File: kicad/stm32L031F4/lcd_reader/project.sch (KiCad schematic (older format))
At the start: 17 parts, among them J1 WAKE, J13 GND_EXT, J2 SWD, J8 RADIO, Q1 CSD16414Q5, U1 74LS14, U2 STM32L031F4Px, U3 74LS14

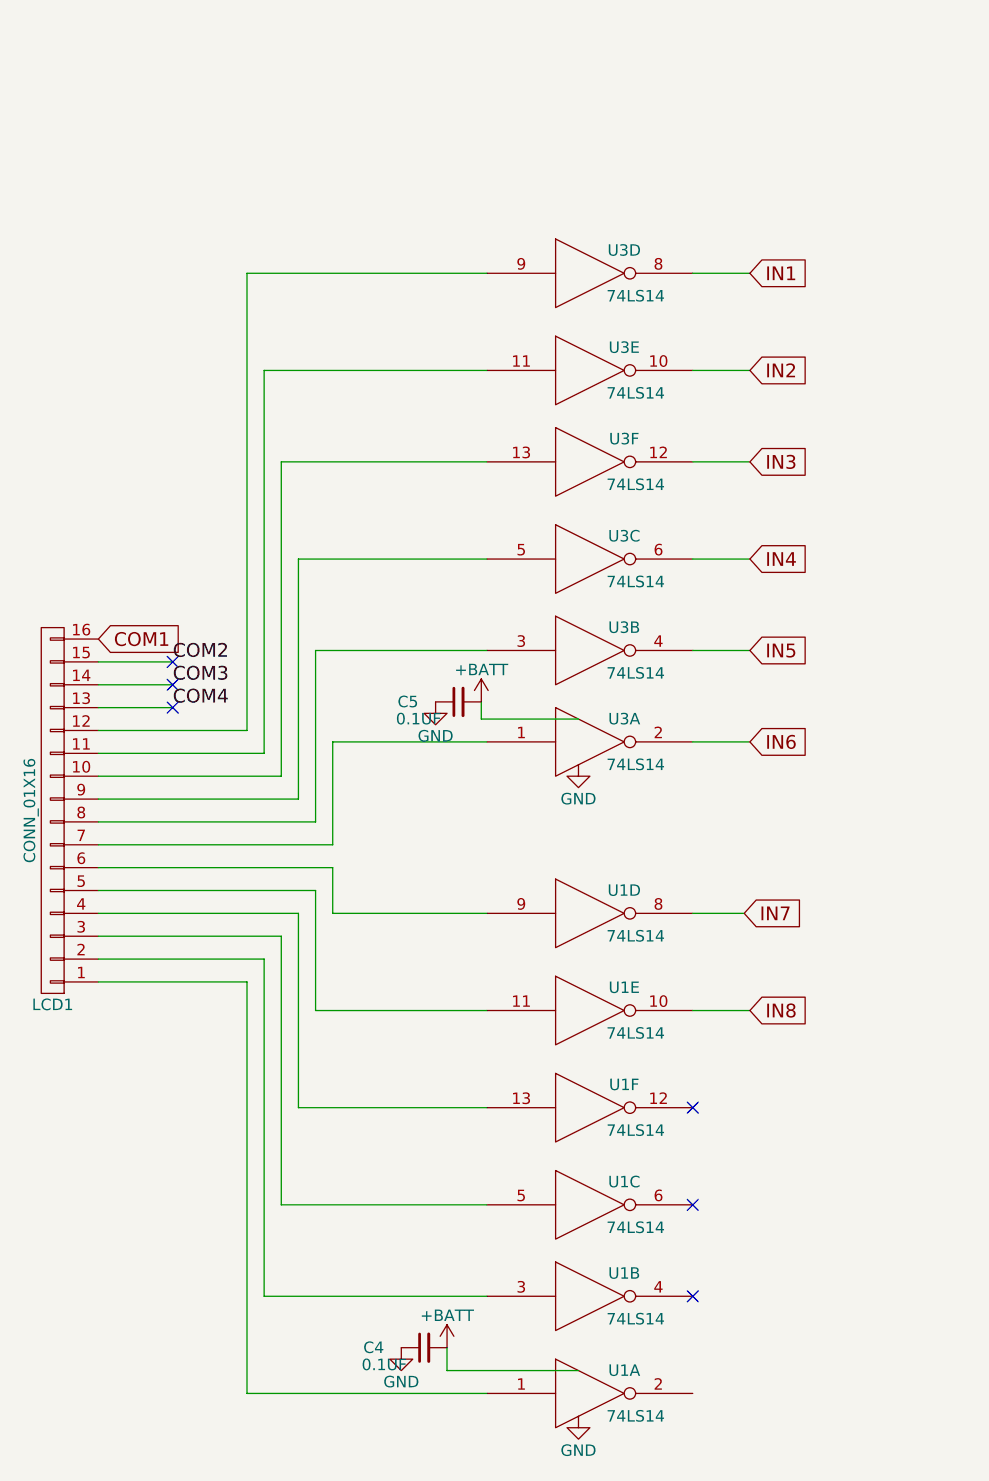
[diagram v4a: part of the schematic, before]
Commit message: SOIC-14 for the schmitt triggers
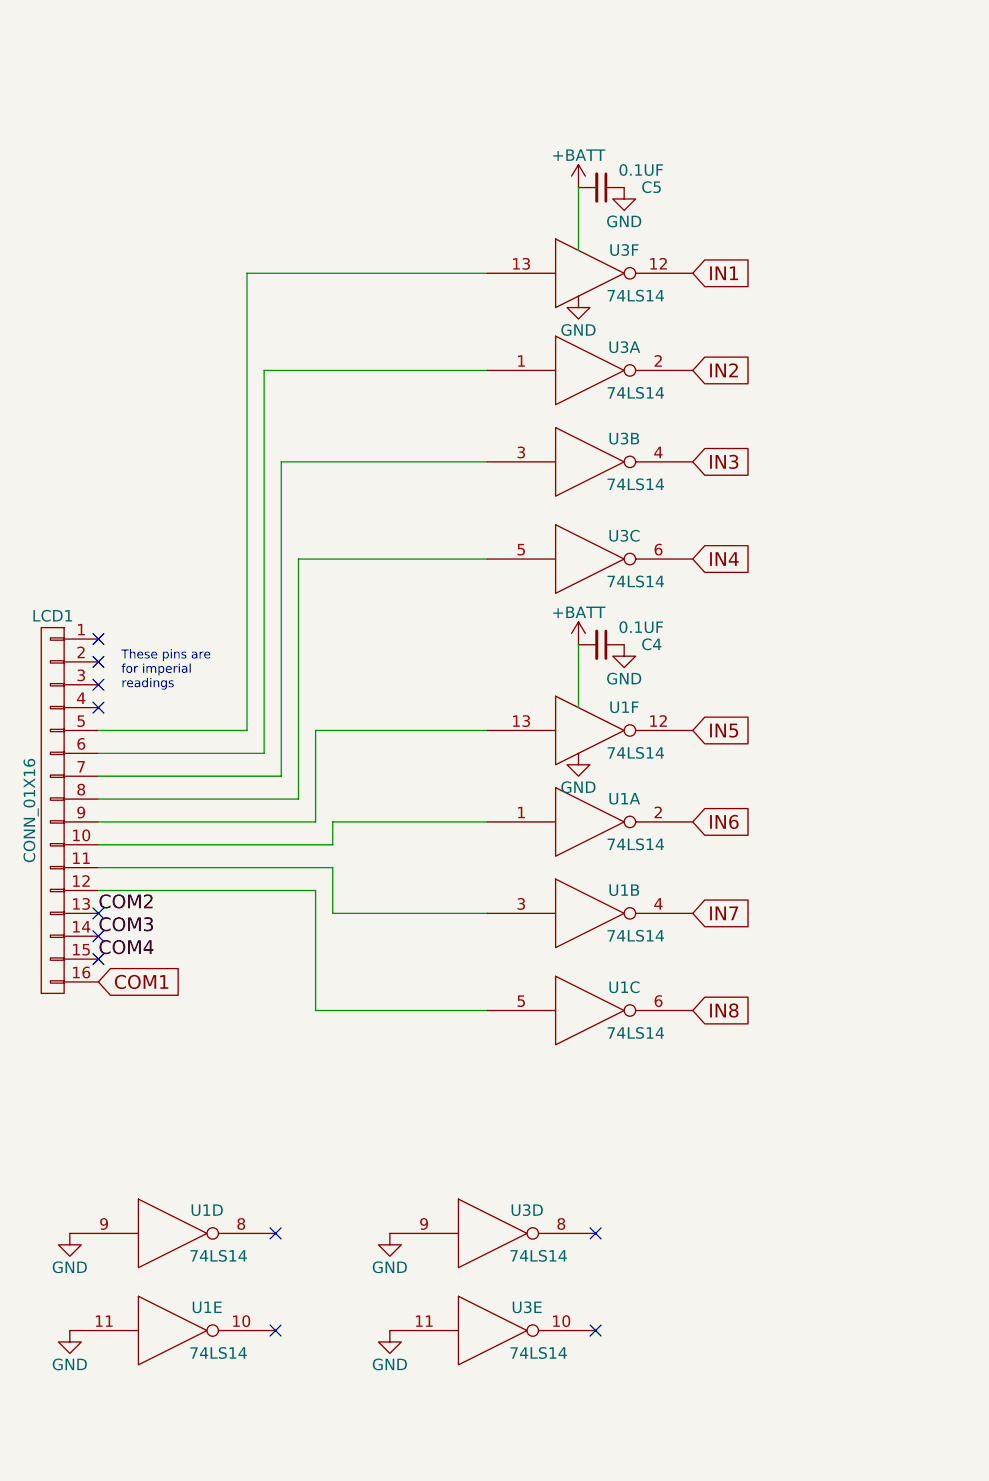
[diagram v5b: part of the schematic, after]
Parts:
- U1, U3: footprint SMD_Packages:SSOP-14 -> Housings_SOIC:SOIC-14_3.9x8.7mm_Pitch1.27mm
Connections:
- net COM2: now also LCD1.13 (P13); no longer LCD1.15 (P15)
- net COM4: now also LCD1.15 (P15); no longer LCD1.13 (P13)
- net GND: now also U1.11, U1.9, U3.11, U3.9
- net IN1: now also U3.12; no longer U3.8
- net IN2: now also U3.2; no longer U3.10
- net IN3: now also U3.4; no longer U3.12
- net IN5: now also U1.12; no longer U3.4
- net IN6: now also U1.2; no longer U3.2
- net IN7: now also U1.4; no longer U1.8
- net IN8: now also U1.6; no longer U1.10
- net at U3.13: now also LCD1.5 (P5); no longer LCD1.10 (P10)
- net at LCD1.11 (P11): now also U1.3; no longer U3.11
- net at LCD1.12 (P12): now also U1.5; no longer U3.9
- net at U3.5: now also LCD1.8 (P8); no longer LCD1.9 (P9)
- net at U1.13: now also LCD1.9 (P9); no longer LCD1.4 (P4)
- net at LCD1.6 (P6): now also U3.1; no longer U1.9
- net at LCD1.3 (P3): no longer U1.5
- net at U3.3: now also LCD1.7 (P7); no longer LCD1.8 (P8)
- net at LCD1.2 (P2): no longer U1.3
- net at U1.1: now also LCD1.10 (P10); no longer LCD1.1 (P1)
- no-connect marks 6 -> 11
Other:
- note added: "These pins are \nfor imperial\nreadings"
- moved on the sheet: C4, C5, U1A, U1B, U1C, U1D, U1E, U1F, U3A, U3B, U3D, U3E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

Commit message: Pull down on mosfet gate
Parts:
- added R3: 10K, Resistors_SMD:R_0805_HandSoldering, symbol R
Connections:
- net GND: now also R3.2
- net at Q1.4 (G), R2.1: now also R3.1
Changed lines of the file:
@@
 $EndComp
 $Comp
-L GND #PWR01
+L GND #PWR14
 U 1 1 5A0070CE
 P 5900 4725
-F 0 "#PWR01" H 5900 4475 50  0001 C CNN
+F 0 "#PWR14" H 5900 4475 50  0001 C CNN
 F 1 "GND" H 5900 4575 50  0000 C CNN
 F 2 "" H 5900 4725 50  0001 C CNN
@@
 $EndComp
 $Comp
-L GND #PWR02
+L GND #PWR16
 U 1 1 5A00715D
 P 6625 5625
-F 0 "#PWR02" H 6625 5375 50  0001 C CNN
+F 0 "#PWR16" H 6625 5375 50  0001 C CNN
 F 1 "GND" H 6625 5475 50  0000 C CNN
 F 2 "" H 6625 5625 50  0001 C CNN
@@
 RADIO_RDY
 $Comp
-L +BATT #PWR03
+L +BATT #PWR8
 U 1 1 5A007816
 P 6575 3125
-F 0 "#PWR03" H 6575 2975 50  0001 C CNN
+F 0 "#PWR8" H 6575 2975 50  0001 C CNN
 F 1 "+BATT" H 6575 3265 50  0000 C CNN
 F 2 "" H 6575 3125 50  0001 C CNN
@@
 $EndComp
 $Comp
-L +BATT #PWR04
+L +BATT #PWR1
 U 1 1 5A007834
 P 7800 1325
-F 0 "#PWR04" H 7800 1175 50  0001 C CNN
+F 0 "#PWR1" H 7800 1175 50  0001 C CNN
 F 1 "+BATT" H 7800 1465 50  0000 C CNN
 F 2 "" H 7800 1325 50  0001 C CNN
@@
 $EndComp
 $Comp
-L GND #PWR05
+L GND #PWR3
 U 1 1 5A00786F
 P 8300 1525
-F 0 "#PWR05" H 8300 1275 50  0001 C CNN
+F 0 "#PWR3" H 8300 1275 50  0001 C CNN
 F 1 "GND" H 8300 1375 50  0000 C CNN
 F 2 "" H 8300 1525 50  0001 C CNN
@@
 $EndComp
 $Comp
-L +BATT #PWR06
+L +BATT #PWR2
 U 1 1 5A007A01
 P 6450 1350
-F 0 "#PWR06" H 6450 1200 50  0001 C CNN
+F 0 "#PWR2" H 6450 1200 50  0001 C CNN
 F 1 "+BATT" H 6450 1490 50  0000 C CNN
 F 2 "" H 6450 1350 50  0001 C CNN
@@
 $EndComp
 $Comp
-L GND #PWR07
+L GND #PWR4
 U 1 1 5A007A1B
 P 6450 1650
-F 0 "#PWR07" H 6450 1400 50  0001 C CNN
+F 0 "#PWR4" H 6450 1400 50  0001 C CNN
 F 1 "GND" H 6450 1500 50  0000 C CNN
 F 2 "" H 6450 1650 50  0001 C CNN
@@
 $EndComp
 $Comp
-L GND #PWR08
+L GND #PWR9
 U 1 1 5A007D44
 P 6325 3325
-F 0 "#PWR08" H 6325 3075 50  0001 C CNN
+F 0 "#PWR9" H 6325 3075 50  0001 C CNN
 F 1 "GND" H 6325 3175 50  0000 C CNN
 F 2 "" H 6325 3325 50  0001 C CNN
@@
 $EndComp
 $Comp
-L GND #PWR09
+L GND #PWR10
 U 1 1 5A007D64
 P 6825 3325
-F 0 "#PWR09" H 6825 3075 50  0001 C CNN
+F 0 "#PWR10" H 6825 3075 50  0001 C CNN
 F 1 "GND" H 6825 3175 50  0000 C CNN
 F 2 "" H 6825 3325 50  0001 C CNN
@@
 $EndComp
 $Comp
-L GND #PWR010
+L GND #PWR15
 U 1 1 5A008B5A
 P 9700 5500
-F 0 "#PWR010" H 9700 5250 50  0001 C CNN
+F 0 "#PWR15" H 9700 5250 50  0001 C CNN
 F 1 "GND" H 9700 5350 50  0000 C CNN
 F 2 "" H 9700 5500 50  0001 C CNN
@@
 $EndComp
 $Comp
-L GND #PWR011
+L GND #PWR12
 U 1 1 5A00DDAB
 P 3775 3875
-F 0 "#PWR011" H 3775 3625 50  0001 C CNN
+F 0 "#PWR12" H 3775 3625 50  0001 C CNN
 F 1 "GND" H 3775 3725 50  0000 C CNN
 F 2 "" H 3775 3875 50  0001 C CNN
@@
 $EndComp
 $Comp
-L GND #PWR012
+L GND #PWR6
 U 1 1 5A00E7EA
 P 3775 1875
-F 0 "#PWR012" H 3775 1625 50  0001 C CNN
+F 0 "#PWR6" H 3775 1625 50  0001 C CNN
 F 1 "GND" H 3775 1725 50  0000 C CNN
 F 2 "" H 3775 1875 50  0001 C CNN
@@
 $EndComp
 $Comp
-L +BATT #PWR013
+L +BATT #PWR5
 U 1 1 5A00EA07
 P 3575 1875
-F 0 "#PWR013" H 3575 1725 50  0001 C CNN
+F 0 "#PWR5" H 3575 1725 50  0001 C CNN
 F 1 "+BATT" H 3575 2015 50  0000 C CNN
 F 2 "" H 3575 1875 50  0001 C CNN
@@
 $EndComp
 $Comp
-L GND #PWR014
+L GND #PWR13
 U 1 1 5A00F77F
 P 3575 4350
-F 0 "#PWR014" H 3575 4100 50  0001 C CNN
+F 0 "#PWR13" H 3575 4100 50  0001 C CNN
 F 1 "GND" H 3575 4200 50  0000 C CNN
 F 2 "" H 3575 4350 50  0001 C CNN
@@
 $EndComp
 $Comp
-L GND #PWR015
+L GND #PWR7
 U 1 1 5A00FAD0
 P 3575 2350
-F 0 "#PWR015" H 3575 2100 50  0001 C CNN
+F 0 "#PWR7" H 3575 2100 50  0001 C CNN
 F 1 "GND" H 3575 2200 50  0000 C CNN
 F 2 "" H 3575 2350 50  0001 C CNN
@@
 NoConn ~ 1475 5250
 $Comp
-L +BATT #PWR016
+L +BATT #PWR11
 U 1 1 5A03249C
 P 3575 3875
-F 0 "#PWR016" H 3575 3725 50  0001 C CNN
+F 0 "#PWR11" H 3575 3725 50  0001 C CNN
 F 1 "+BATT" H 3575 4015 50  0000 C CNN
 F 2 "" H 3575 3875 50  0001 C CNN
@@
 Wire Wire Line
 	9700 4750 9700 4025
-Wire Wire Line
-	9400 5350 8875 5350
 Wire Wire Line
 	9700 5350 9700 5500
@@
 	2425 4250 2425 4650
 $Comp
-L GND #PWR017
+L GND #PWR18
 U 1 1 5A04DF95
 P 1350 6450
-F 0 "#PWR017" H 1350 6200 50  0001 C CNN
+F 0 "#PWR18" H 1350 6200 50  0001 C CNN
 F 1 "GND" H 1350 6300 50  0000 C CNN
 F 2 "" H 1350 6450 50  0001 C CNN
@@
 $EndComp
 $Comp
-L GND #PWR018
+L GND #PWR20
 U 1 1 5A04E027
 P 1350 6875
-F 0 "#PWR018" H 1350 6625 50  0001 C CNN
+F 0 "#PWR20" H 1350 6625 50  0001 C CNN
 F 1 "GND" H 1350 6725 50  0000 C CNN
 F 2 "" H 1350 6875 50  0001 C CNN
@@
 NoConn ~ 2250 6875
 $Comp
-L GND #PWR019
+L GND #PWR19
 U 1 1 5A04EFD4
 P 2750 6450
-F 0 "#PWR019" H 2750 6200 50  0001 C CNN
+F 0 "#PWR19" H 2750 6200 50  0001 C CNN
 F 1 "GND" H 2750 6300 50  0000 C CNN
 F 2 "" H 2750 6450 50  0001 C CNN
@@
 $EndComp
 $Comp
-L GND #PWR020
+L GND #PWR21
 U 1 1 5A04F030
 P 2750 6875
-F 0 "#PWR020" H 2750 6625 50  0001 C CNN
+F 0 "#PWR21" H 2750 6625 50  0001 C CNN
 F 1 "GND" H 2750 6725 50  0000 C CNN
 F 2 "" H 2750 6875 50  0001 C CNN
@@
 Wire Wire Line
 	3575 3875 3575 4150
+$Comp
+L R R3
+U 1 1 5A38EF65
+P 9025 5500
+F 0 "R3" V 9105 5500 50  0000 C CNN
+F 1 "10K" V 9025 5500 50  0000 C CNN
+F 2 "Resistors_SMD:R_0805_HandSoldering" V 8955 5500 50  0001 C CNN
+F 3 "" H 9025 5500 50  0001 C CNN
+	1    9025 5500
+	1    0    0    -1
+$EndComp
+Wire Wire Line
+	8875 5350 9400 5350
+Connection ~ 9025 5350
+$Comp
+L GND #PWR17
+U 1 1 5A38F119
+P 9025 5650
+F 0 "#PWR17" H 9025 5400 50  0001 C CNN
+F 1 "GND" H 9025 5500 50  0000 C CNN
+F 2 "" H 9025 5650 50  0001 C CNN
+F 3 "" H 9025 5650 50  0001 C CNN
+	1    9025 5650
+	1    0    0    -1
+$EndComp
 $EndSCHEMATC
